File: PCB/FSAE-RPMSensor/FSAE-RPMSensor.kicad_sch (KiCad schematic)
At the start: 4 parts, among them J1 Conn_01x02_Pin, J2 Conn_01x02_Pin

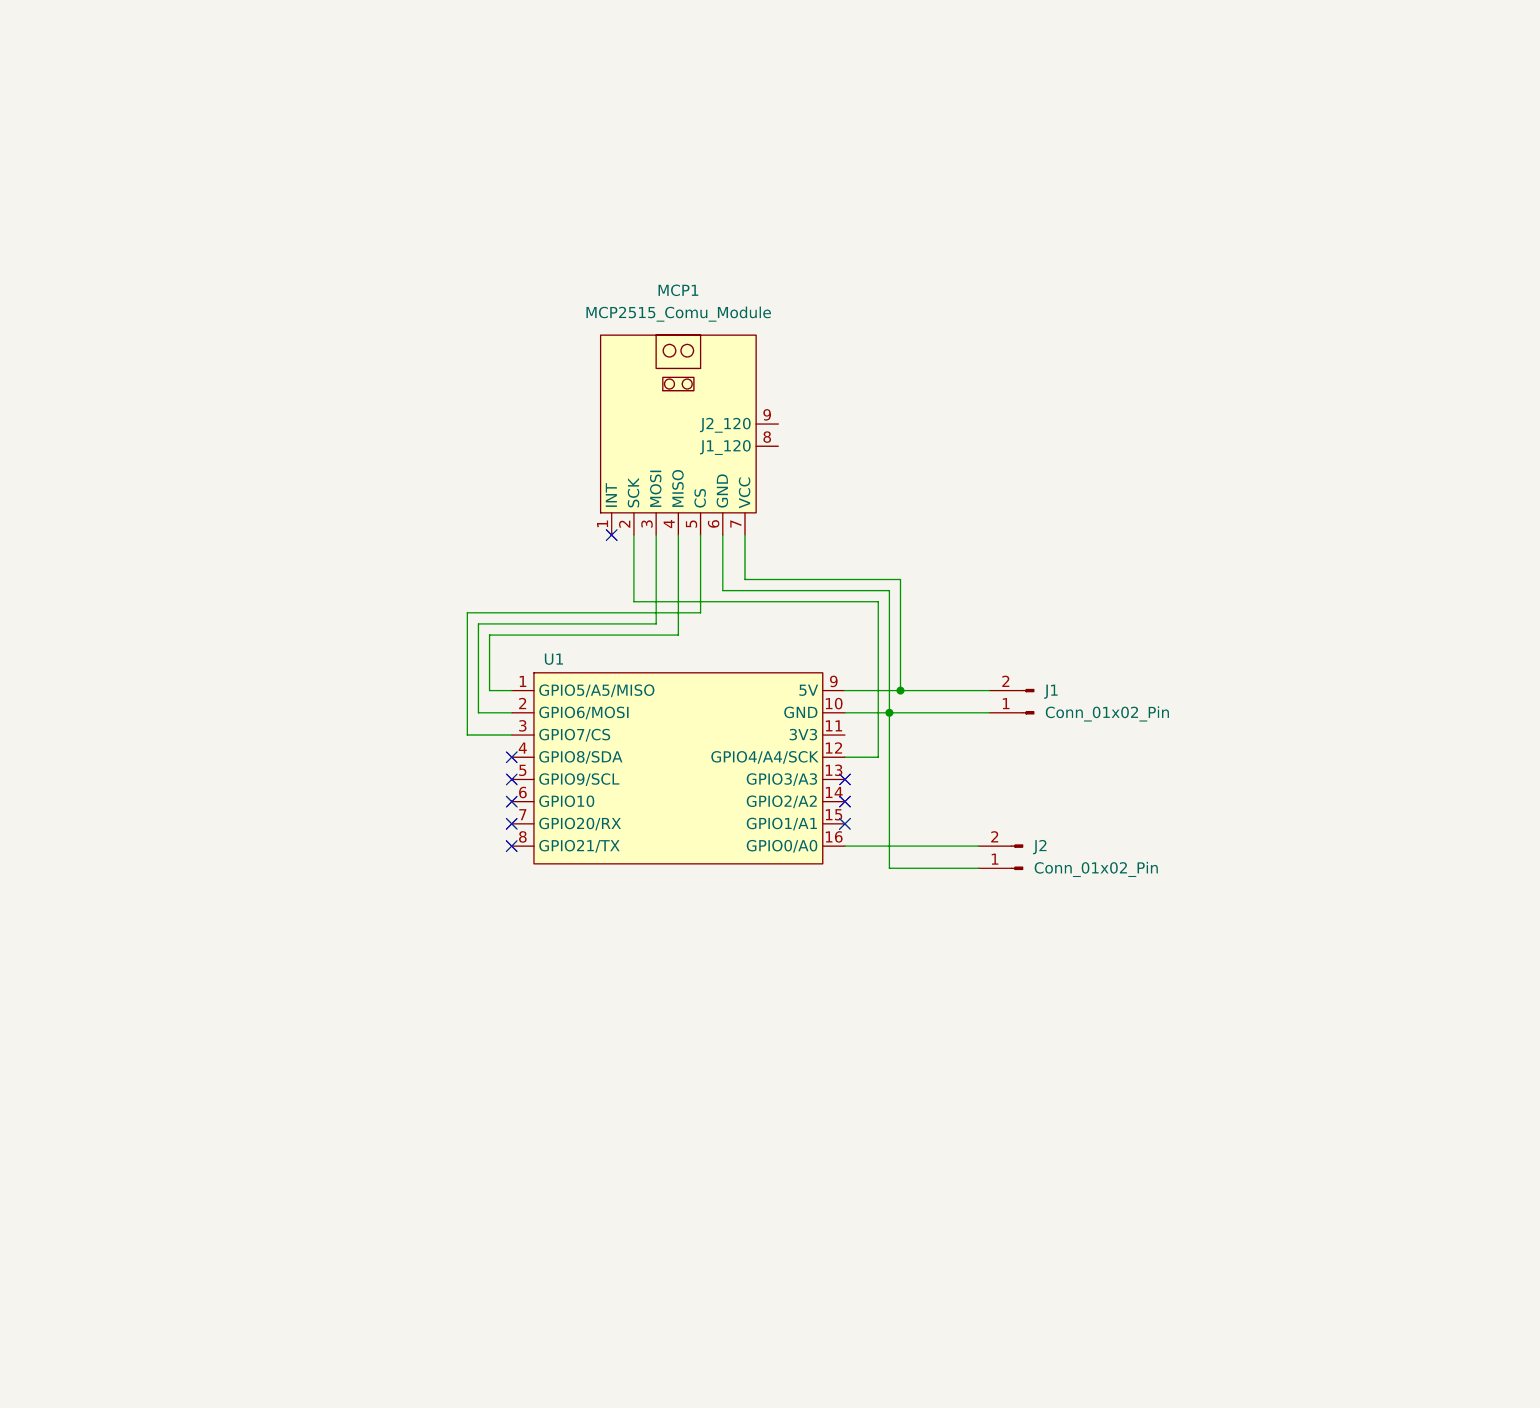
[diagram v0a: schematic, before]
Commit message: Modificacion de la placa pcb del modelo de comunicacion CAN por uno aisaldo y con fuente buck para el ESP32 C3
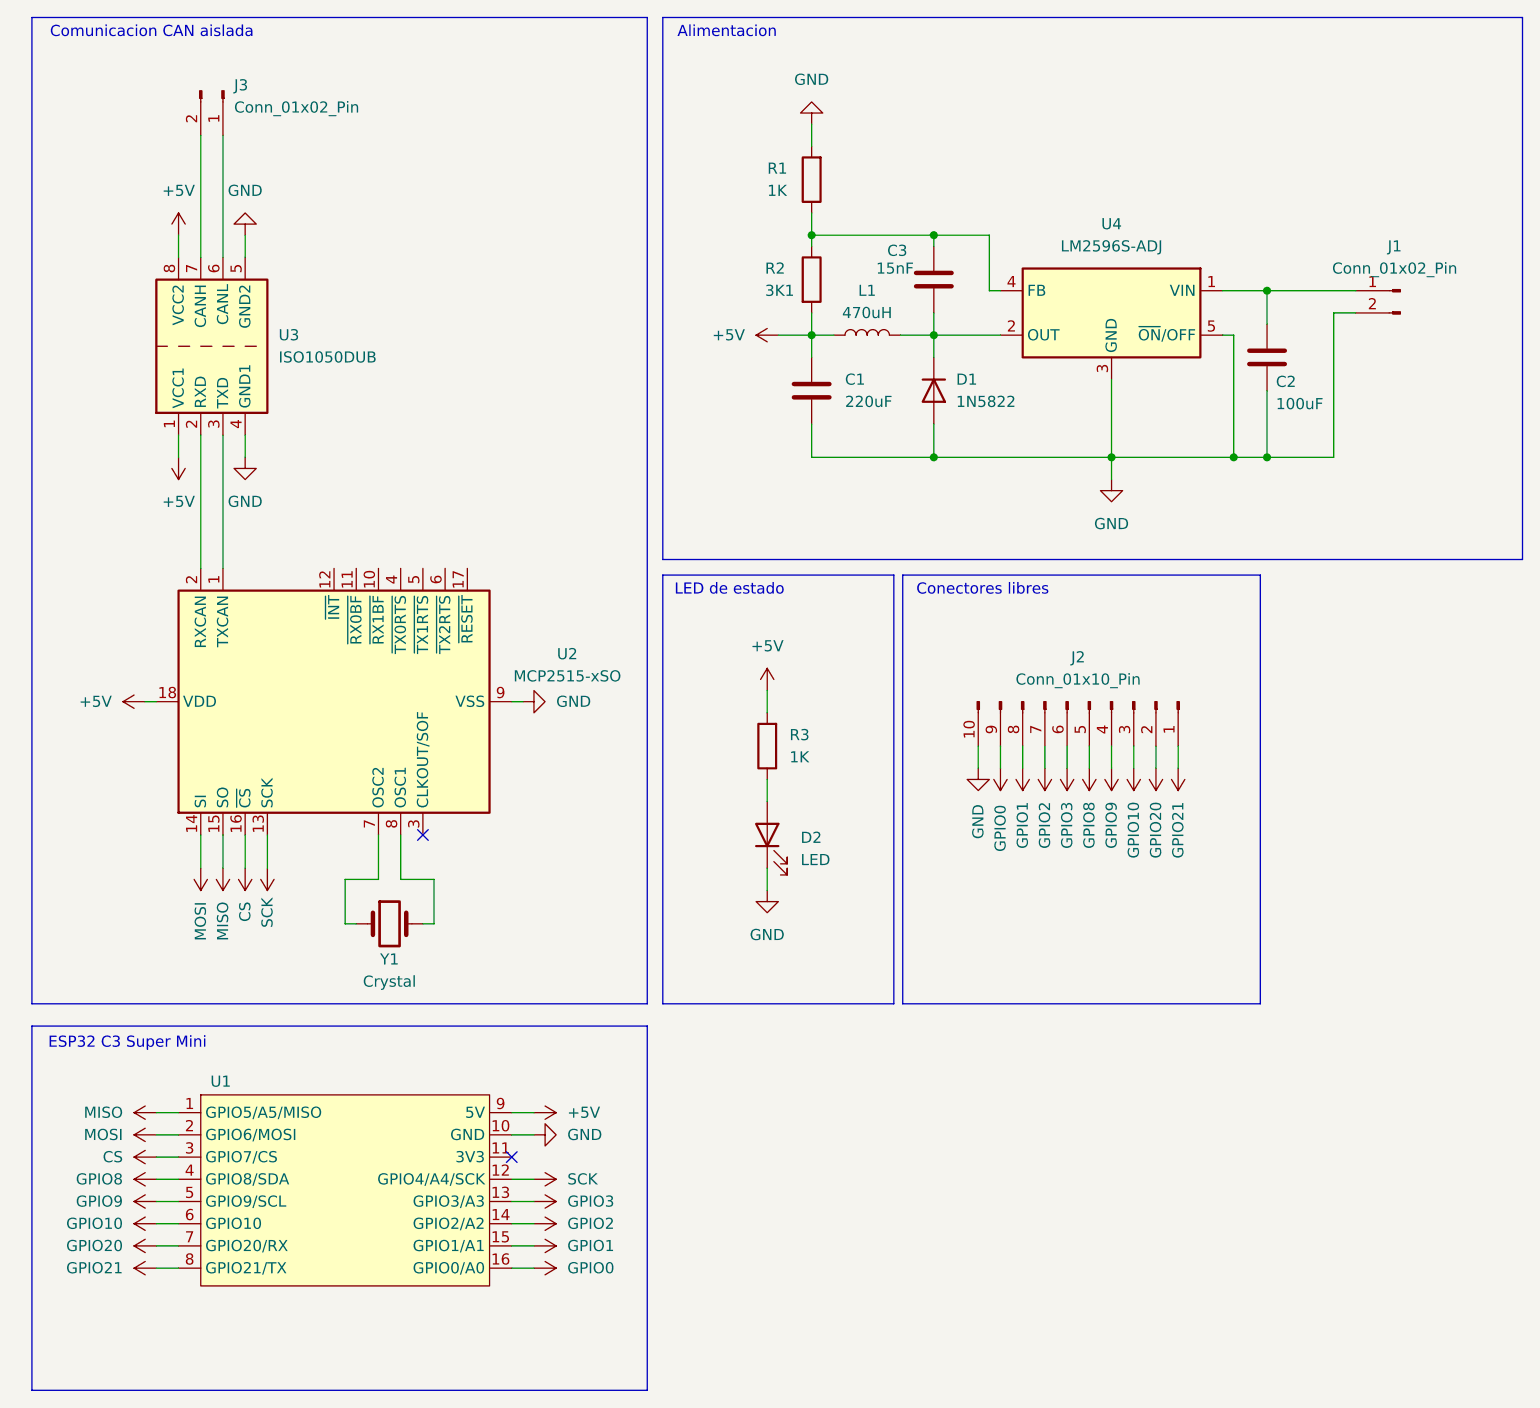
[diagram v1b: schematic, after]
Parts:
- removed J2: Conn_01x02_Pin, Connector_AMASS:AMASS_XT30U-F_1x02_P5.0mm_Vertical, symbol Connector:Conn_01x02_Pin
- removed MCP1: MCP2515_Comu_Module, FSAE_Library:MCP2515_Comun_Module, symbol FSAE_Library:MCP2515_Comu_Module
- added C1: 220uF, Capacitor_SMD:C_Elec_8x5.4, symbol Device:C
- added C2: 100uF, Capacitor_SMD:C_Elec_8x5.4, symbol Device:C
- added C3: 15nF, Capacitor_SMD:C_0603_1608Metric, symbol Device:C
- added D1: 1N5822, Diode_SMD:D_1206_3216Metric, symbol Device:D
- added D2: LED, Diode_SMD:D_0603_1608Metric, symbol Device:LED
- added J2: Conn_01x10_Pin, Connector_PinHeader_1.00mm:PinHeader_1x10_P1.00mm_Vertical, symbol Connector:Conn_01x10_Pin
- added J3: Conn_01x02_Pin, Connector_AMASS:AMASS_XT30U-F_1x02_P5.0mm_Vertical, symbol Connector:Conn_01x02_Pin
- added L1: 470uH, Inductor_SMD:L_10.4x10.4_H4.8, symbol Device:L
- added R1, R3: 1K, Resistor_SMD:R_0603_1608Metric, symbol Device:R
- added R2: 3K1, Resistor_SMD:R_0603_1608Metric, symbol Device:R
- added U2: MCP2515-xSO, Package_SO:SOIC-18W_7.5x11.6mm_P1.27mm, symbol Interface_CAN_LIN:MCP2515-xSO
- added U3: ISO1050DUB, Package_SO:SOP-8_6.62x9.15mm_P2.54mm, symbol Interface_CAN_LIN:ISO1050DUB
- added U4: LM2596S-ADJ, Package_TO_SOT_SMD:TO-263-5_TabPin3, symbol Regulator_Switching:LM2596S-ADJ
- added Y1: Crystal, Crystal:Crystal_HC18-U_Vertical, symbol Device:Crystal
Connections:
- net at J1.1 (Pin_1): now also C2.1, U4.1 (VIN); no longer U1.10 (GND)
- net +5V: now reaches U1.9 (5V)
- net +5V: now also C1.1, L1.1, R2.2, R3.2, U2.18 (VDD), U3.1 (VCC1), U3.8 (VCC2); no longer J1.2 (Pin_2)
- net MISO: now reaches U1.1 (GPIO5/A5/MISO)
- net MISO: now also U2.15 (SO)
- net SCK: now reaches U1.12 (GPIO4/A4/SCK)
- net SCK: now also U2.13 (SCK)
- net GPIO3: now reaches U1.13 (GPIO3/A3)
- net GPIO3: now also J2.6 (Pin_6)
- net GPIO2: now reaches U1.14 (GPIO2/A2)
- net GPIO2: now also J2.7 (Pin_7)
- net GPIO1: now reaches U1.15 (GPIO1/A1)
- net GPIO1: now also J2.8 (Pin_8)
- net GPIO0: now reaches U1.16 (GPIO0/A0)
- net GPIO0: now also J2.9 (Pin_9)
- net MOSI: now reaches U1.2 (GPIO6/MOSI)
- net MOSI: now also U2.14 (SI)
- net CS: now reaches U1.3 (GPIO7/CS)
- net CS: now also U2.16 (~{CS})
- net GPIO8: now reaches U1.4 (GPIO8/SDA)
- net GPIO8: now also J2.5 (Pin_5)
- net GPIO9: now reaches U1.5 (GPIO9/SCL)
- net GPIO9: now also J2.4 (Pin_4)
- net GPIO10: now reaches U1.6 (GPIO10)
- net GPIO10: now also J2.3 (Pin_3)
- net GPIO20: now reaches U1.7 (GPIO20/RX)
- net GPIO20: now also J2.2 (Pin_2)
- net GPIO21: now reaches U1.8 (GPIO21/TX)
- net GPIO21: now also J2.1 (Pin_1)
- new net: D2.2 (A), R3.1
- new net: C3.1, R1.1, R2.1, U4.4 (FB)
- new net: U2.1 (TXCAN), U3.3 (TXD)
- new net: U2.2 (RXCAN), U3.2 (RXD)
- new net: U2.7 (OSC2), Y1.1
- new net: U2.8 (OSC1), Y1.2
- new net: C3.2, D1.1 (K), L1.2, U4.2 (OUT)
- new net: J3.1 (Pin_1), U3.6 (CANL)
- new net: J3.2 (Pin_2), U3.7 (CANH)
- new net GND: C1.2, C2.2, D1.2 (A), D2.1 (K), J1.2 (Pin_2), J2.10 (Pin_10), R1.2, U1.10 (GND), U2.9 (VSS), U3.4 (GND1), U3.5 (GND2), U4.3 (GND), U4.5 (~{ON}/OFF)
- no-connect marks 9 -> 2
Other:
- note added: "Alimentacion"
- note added: "Comunicacion CAN aislada"
- note added: "Conectores libres"
- note added: "ESP32 C3 Super Mini"
- note added: "LED de estado"
- moved on the sheet: J1, U1
